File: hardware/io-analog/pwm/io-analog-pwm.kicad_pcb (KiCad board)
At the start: 2 copper layers, 69.1 x 53.8 mm, 10 parts, among them J1 Output, J2 INPUT

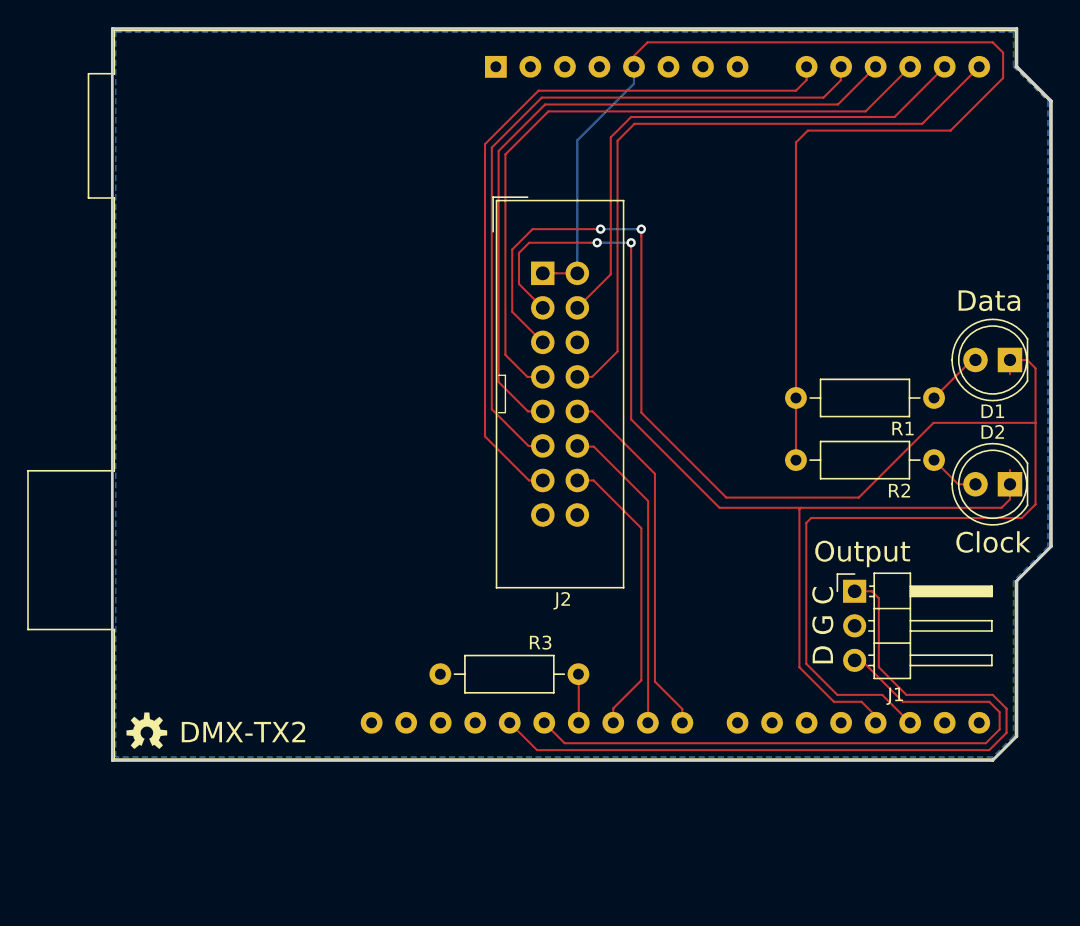
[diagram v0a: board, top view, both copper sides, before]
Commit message: Prototype version of DMX, Analog, and PWM IO Modules and both TX and RX IO interfaces.
Make io-analog a stackable family
io-analog-core handles D to A
io-analog-voltage handles voltage output
io-analog-pwm handles pwm output for leds, drive display pro

Refactor display-pro to work with io-analog-pwm
Add correct coax power connector

Move TX2 to tx-io
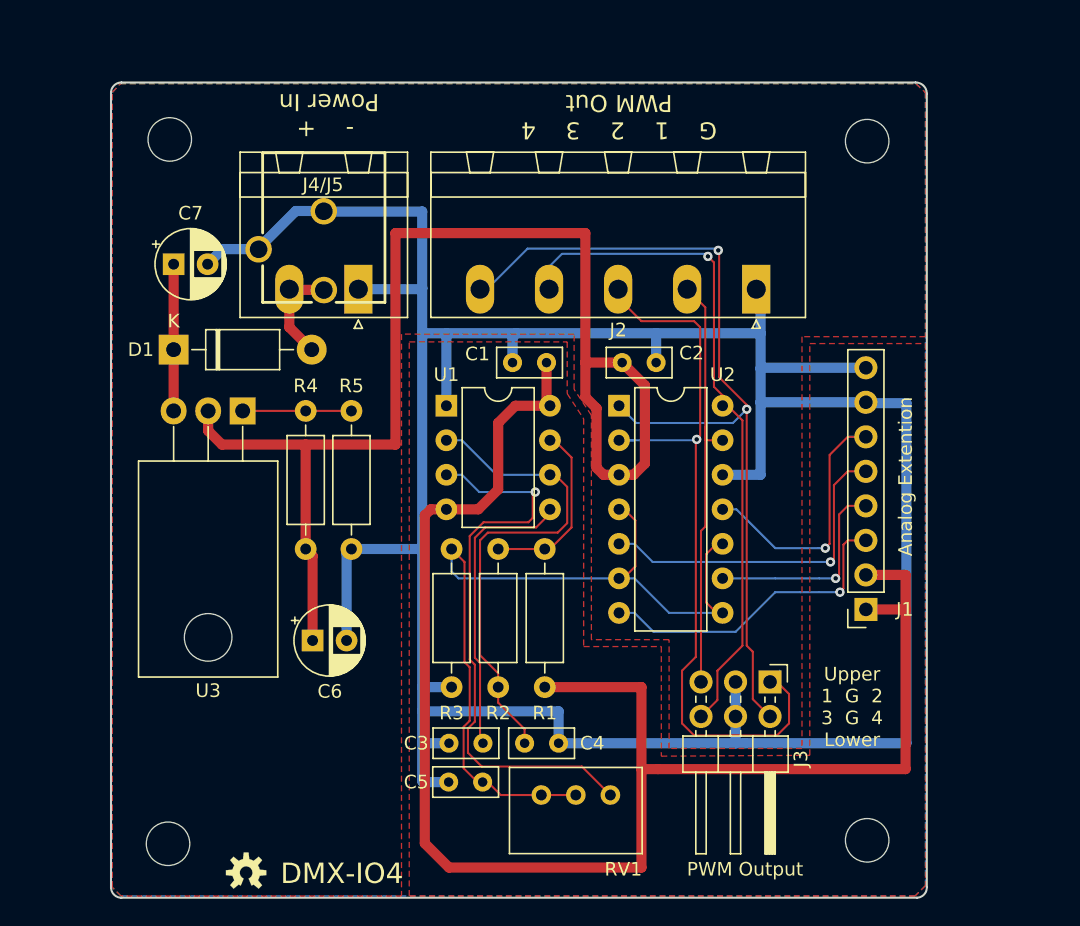
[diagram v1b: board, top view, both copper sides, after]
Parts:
- removed the ? at (118.9, 114.8)
- removed A1: Arduino_UNO_R3, Module:Arduino_UNO_R3
- removed D2: CLOCK, LED_THT:LED_D5.0mm
- added ?: , footprints:OSHW-LOGO-S, F.Cu at (126.2, 125.1)
- added C1: 0.1uF, Capacitor_THT:C_Rect_L4.6mm_W2.0mm_P2.50mm_MKS02_FKP02, F.Cu at (148.3, 87.6)
- added C2: 0.1uF, Capacitor_THT:C_Rect_L4.6mm_W2.0mm_P2.50mm_MKS02_FKP02, F.Cu at (153.8, 87.6)
- added C3: 100nf, Capacitor_THT:C_Rect_L4.6mm_W2.0mm_P2.50mm_MKS02_FKP02, F.Cu at (141.1, 115.6)
- added C4: 0.68uF, Capacitor_THT:C_Rect_L4.6mm_W2.0mm_P2.50mm_MKS02_FKP02, F.Cu at (149.2, 115.6)
- added C5: 0.68uF, Capacitor_THT:C_Rect_L4.6mm_W2.0mm_P2.50mm_MKS02_FKP02, F.Cu at (143.6, 118.4)
- added C6: 10uF, Capacitor_THT:CP_Radial_D5.0mm_P2.50mm, F.Cu at (131.1, 108.0)
- added C7: 10uF, Capacitor_THT:CP_Radial_D5.0mm_P2.50mm, F.Cu at (120.8, 80.3)
- added J3: Output, Connector_PinHeader_2.54mm:PinHeader_2x03_P2.54mm_Horizontal, F.Cu at (164.7, 111.1)
- added J4: Power, Connector_Phoenix_MSTB:PhoenixContact_MSTBA_2,5_2-G-5,08_1x02_P5.08mm_Horizontal, F.Cu at (134.4, 82.2)
- added J5: Power, Connectors:POWER_JACK_PTH_BREAD, F.Cu at (131.9, 68.5)
- added MH1: MountingHole, MountingHole:MountingHole_3.2mm_M3, F.Cu at (120.6, 71.2)
- added MH2: MountingHole, MountingHole:MountingHole_3.2mm_M3, F.Cu at (171.9, 71.3)
- added MH3: MountingHole, MountingHole:MountingHole_3.2mm_M3, F.Cu at (120.4, 123.0)
- added MH4: MountingHole, MountingHole:MountingHole_3.2mm_M3, F.Cu at (171.9, 122.7)
- added R4: 392 1%, Resistor_THT:R_Axial_DIN0207_L6.3mm_D2.5mm_P10.16mm_Horizontal, F.Cu at (130.6, 91.1)
- added R5: 2.74k 1%, Resistor_THT:R_Axial_DIN0207_L6.3mm_D2.5mm_P10.16mm_Horizontal, F.Cu at (133.9, 101.3)
- added RV1: 10k, Potentiometer_THT:Potentiometer_Bourns_3299W_Vertical, F.Cu at (153.0, 119.4)
- added U1: LM555, Package_DIP:DIP-8_W7.62mm, F.Cu at (140.9, 90.7)
- added U2: LM339, Package_DIP:DIP-14_W7.62mm, F.Cu at (153.6, 90.7)
- added U3: LM317T, Package_TO_SOT_THT:TO-220-3_Horizontal_TabDown, F.Cu at (125.9, 91.1)
- D1: value DATA -> 1N5819; footprint LED_THT:LED_D5.0mm -> Diode_THT:D_DO-41_SOD81_P10.16mm_Horizontal
- J1: value Output -> Analog Extension; footprint Connector_PinHeader_2.54mm:PinHeader_1x03_P2.54mm_Horizontal -> Connector_PinSocket_2.54mm:PinSocket_1x08_P2.54mm_Vertical
- J2: value INPUT -> Output; footprint Connector_IDC:IDC-Header_2x08_P2.54mm_Vertical -> Connector_Phoenix_MSTB:PhoenixContact_MSTBA_2,5_5-G-5,08_1x05_P5.08mm_Horizontal
- R2, R3: value 330 -> 10k
- moved D1 61.5 mm to (120.8, 86.6), turned to 0 degrees
- moved R1 28.2 mm to (148.1, 111.4), turned to 90 degrees
- moved R2 22.9 mm to (144.7, 101.3), turned to 270 degrees
- moved J2 15.7 mm to (163.7, 82.2), turned to 180 degrees
- moved G*** 14.3 mm to (127.0, 122.5)
- moved R3 9.38 mm to (141.3, 111.4), turned to 90 degrees
- moved J1 1.57 mm to (171.8, 105.7), turned to 180 degrees
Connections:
- D1 pad 1: /~DATA -> Net-(C7-Pad1)
- J1 pad 1: /RXCLK -> +5V
- J1 pad 2: GND -> +5V
- J1 pad 3: /RX -> /AO3
- J2 pad 1: +5V -> GND
- J2 pad 2: +5V -> Net-(J2-Pad2)
- J2 pad 3: /~CLOCK -> Net-(J2-Pad3)
- J2 pad 4: /A4 -> Net-(J2-Pad4)
- J2 pad 5: /~DATA -> Net-(J2-Pad5)
- R1 pad 2: Net-(D1-Pad2) -> Net-(R1-Pad2)
- R2 pad 1: +5V -> Net-(R1-Pad2)
- R3 pad 1: Net-(A1-Pad26) -> GND
- R3 pad 2: GND -> Net-(C5-Pad1)
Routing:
- net GND: track 0.00 -> 220.0 mm
- net /~DATA: track 115.7 -> 0.00 mm, vias 2 -> 0
- net Net-(C2-Pad1): track 0.00 -> 92.5 mm
- net /~CLOCK: track 78.7 -> 0.00 mm, vias 2 -> 0
- net Net-(J2-Pad5): track 0.00 -> 65.0 mm, vias 0 -> 2
- net Net-(C5-Pad1): track 0.00 -> 61.9 mm
- net Net-(J2-Pad3): track 0.00 -> 57.5 mm, vias 0 -> 1
- net /RXCLK: track 57.4 -> 0.00 mm
- net /A0: track 53.7 -> 0.00 mm
- net /A1: track 52.9 -> 0.00 mm
- net /A2: track 51.4 -> 0.00 mm
- net /A3: track 50.6 -> 0.00 mm
- net Net-(J2-Pad4): track 0.00 -> 50.2 mm, vias 0 -> 1
- net /A5: track 48.1 -> 0.00 mm
- net /RX: track 48.1 -> 0.00 mm
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- added copper zone on F.Cu, net +5V
- added copper zone on F.Cu, net Net-(C2-Pad1)
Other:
- board size 69.1 x 53.8 mm -> 60 x 60 mm
- net class Power added: clearance 0.25, trace_width 0.75, via_dia 1.27, via_drill 0.635
- board text added: "- + Power In"
- board text added: "Analog Extention"
- board text added: "DMX-IO4"
- board text added: "DMX-IO4, Rev 1.2 Crazy Giraffe Software"
- board text added: "G 1 2 3 4 PWM Out"
- board text added: "J4/J5"
- board text added: "PWM Output"
- board text added: "Upper 1 G 2 3 G 4 Lower"
- board text removed: "Clock"
- board text removed: "D G C"
- board text removed: "DMX-TX2"
- board text removed: "DMX-TX2, Rev 1.0 Crazy Giraffe Software"
- board text removed: "Data"
- board text removed: "Output"
